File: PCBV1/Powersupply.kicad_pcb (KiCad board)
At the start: 4 copper layers, 145 x 99.1 mm, 136 parts, among them J1 Conn_01x02, J2 Conn_WallPlug, J3 QSH-030-01-F-D-A-K-TR, J4 M50-3610742, J5 Conn_01x02, J6 Conn_01x02, J7 Conn_01x02, J8 Conn_01x07, J9 Conn_01x03, T1 EFD 20/10/7, U1 ST1S41PHR, U2 ST1S41PHR, U3 VIPER318HDTR, U4 STM32F469IITx, U5 IS42S16400J-xT, U6 W25Q32JVSS, X1 ECS-5032MV-100-CN-TR

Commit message: Final fixes to PCB silk screen and via layout.
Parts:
- moved R8 0.52 mm to (186.2, 109.3)
- moved R7 0.38 mm to (184.7, 109.3)
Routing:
- net Net-(R5-Pad1): track 35.4 -> 4.32 mm
- net Net-(C18-Pad1): track 11.0 -> 11.5 mm
- net GNDREF: vias 50 -> 62
- net GND: vias 238 -> 284
- added copper zone on F.Cu, net Net-(R5-Pad1)
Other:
- board text added: "Bluetooth"

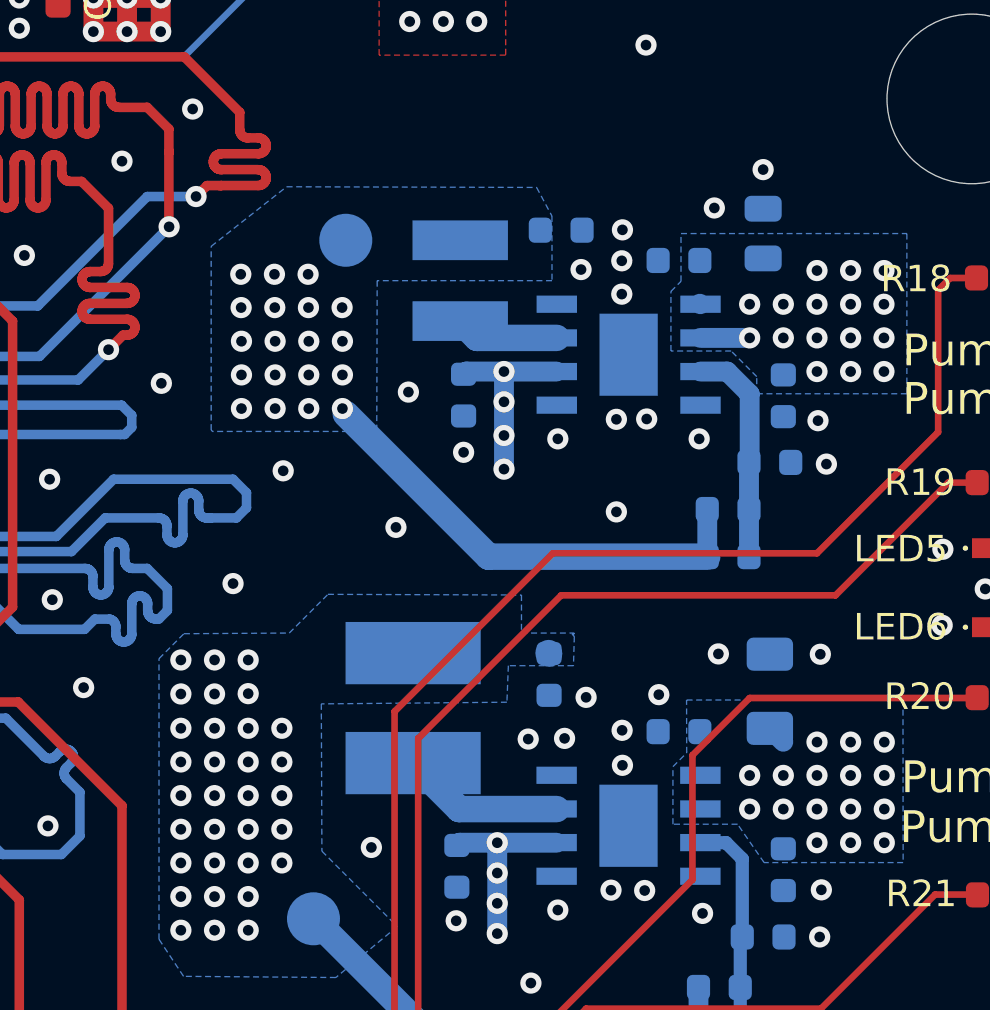
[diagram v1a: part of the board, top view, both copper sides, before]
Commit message: Alterations to voltage regulator circuits for improved performance.
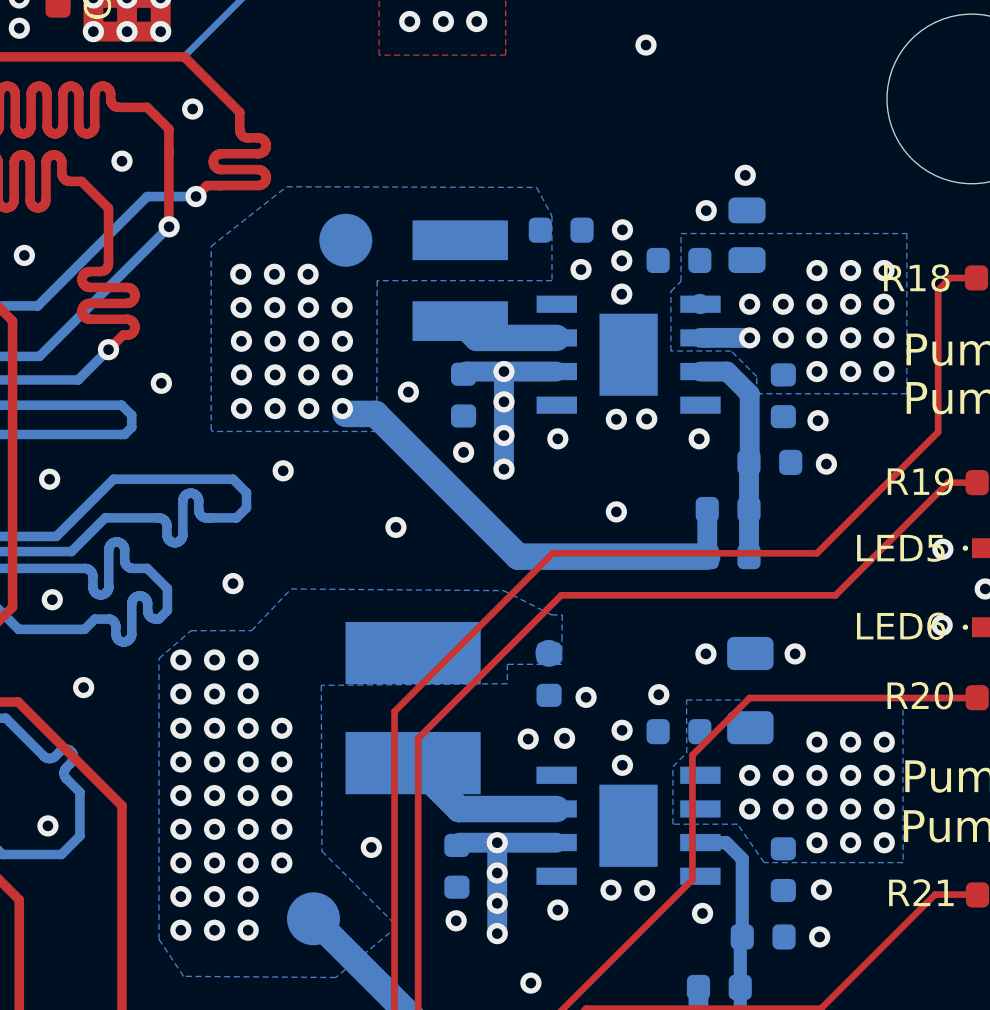
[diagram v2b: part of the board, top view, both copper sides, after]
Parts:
- moved C1 0.74 mm to (200.7, 60.4)
- moved C7 0.61 mm to (200.6, 43.2)
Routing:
- net 12V: track 19.1 -> 18.3 mm
